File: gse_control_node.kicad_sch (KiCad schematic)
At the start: 5 parts

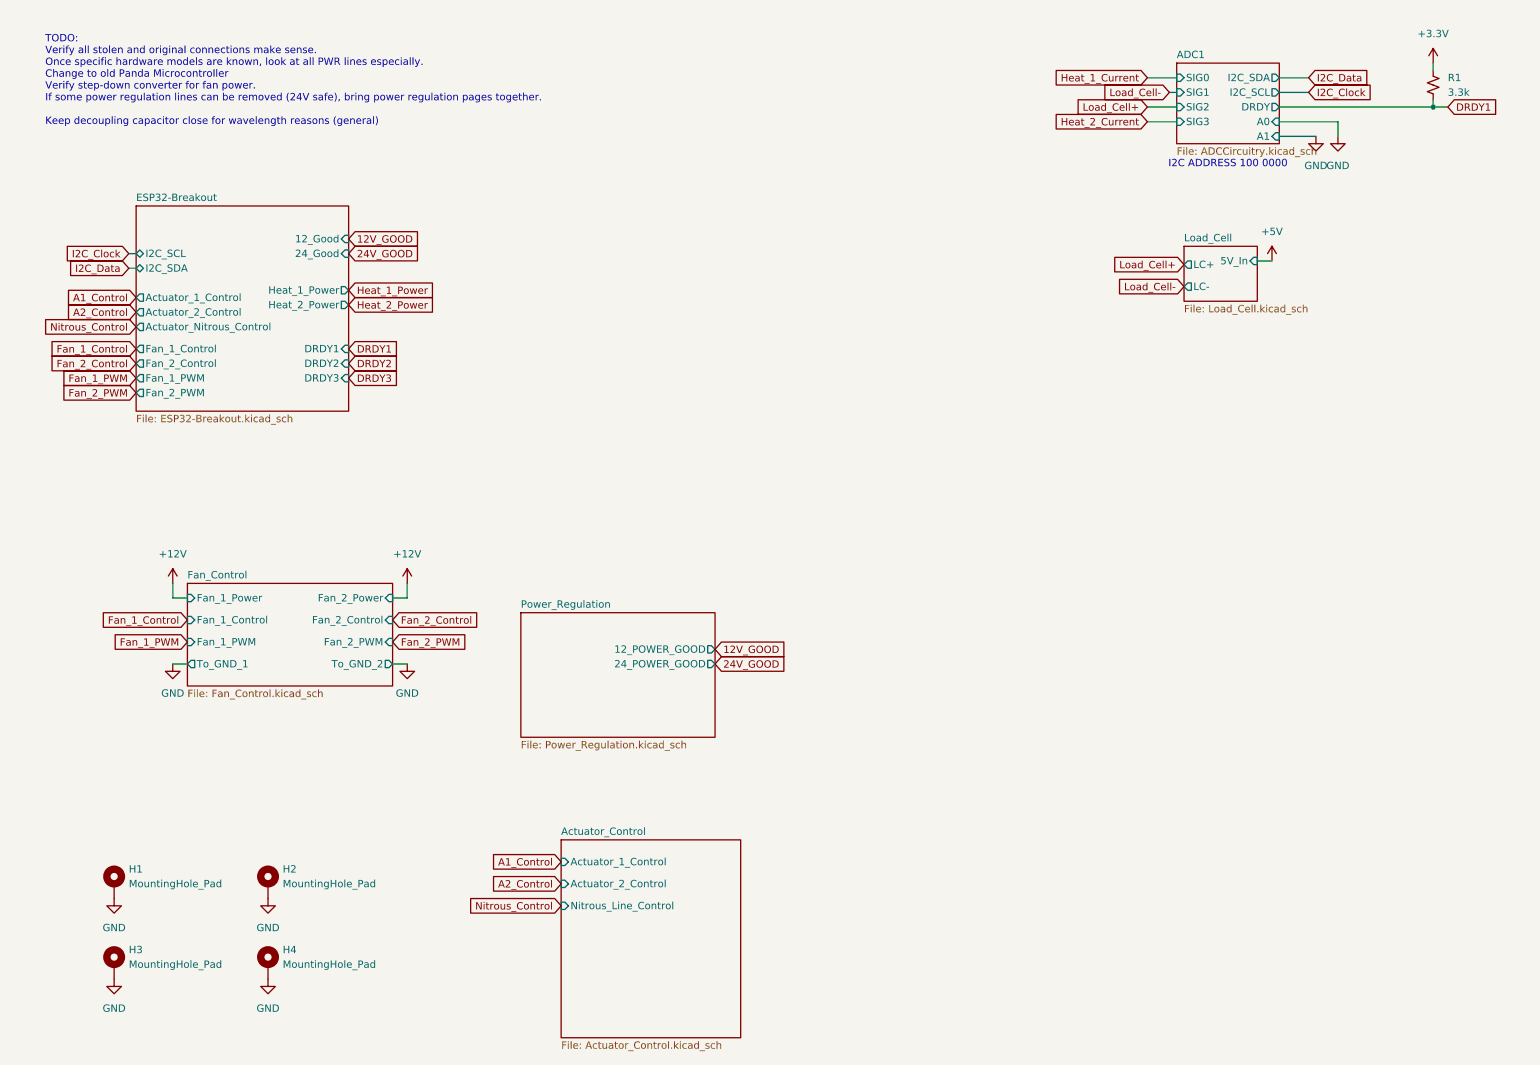
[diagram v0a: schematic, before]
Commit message: rename project to be more descriptive
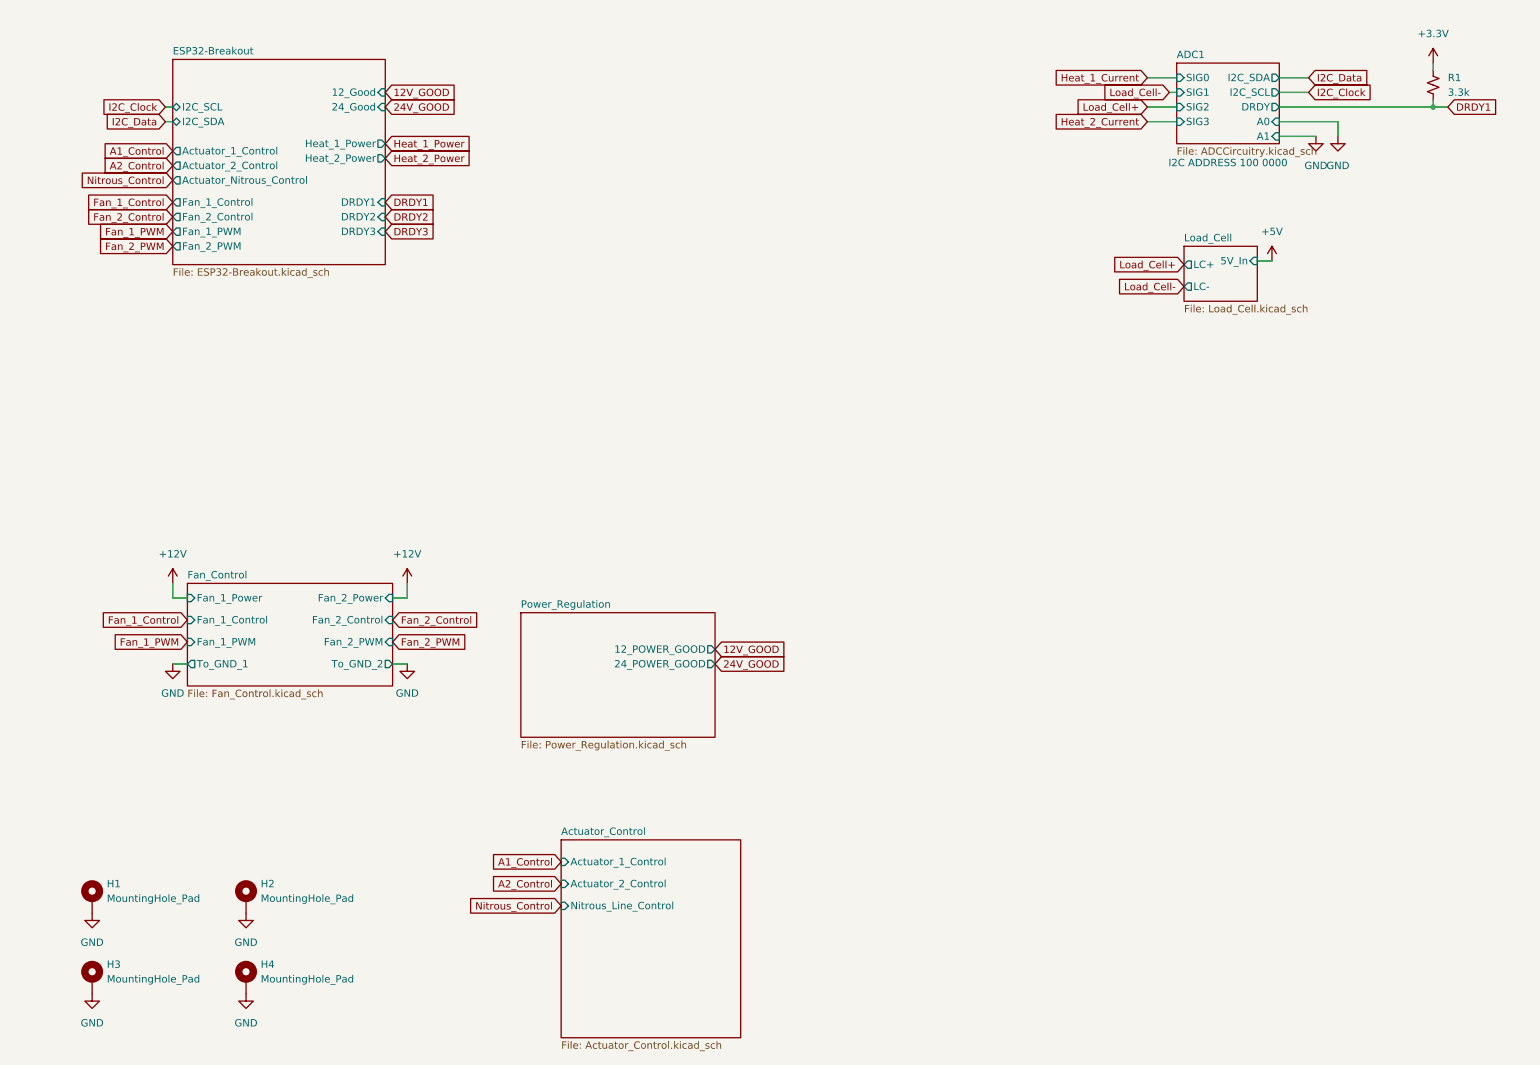
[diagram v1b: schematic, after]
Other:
- note removed: "TODO: Verify all stolen and original connections make sense. Once specific hardware models are known, look at all PWR lines especially. Change to old Panda Microcontroller Verify step-down converter for fan power. If some power regulation lines can be removed (24V safe), bring power regulation pages together. Keep decoupling capacitor close for wavelength reasons (general)"
- moved on the sheet: H1, H2, H3, H4

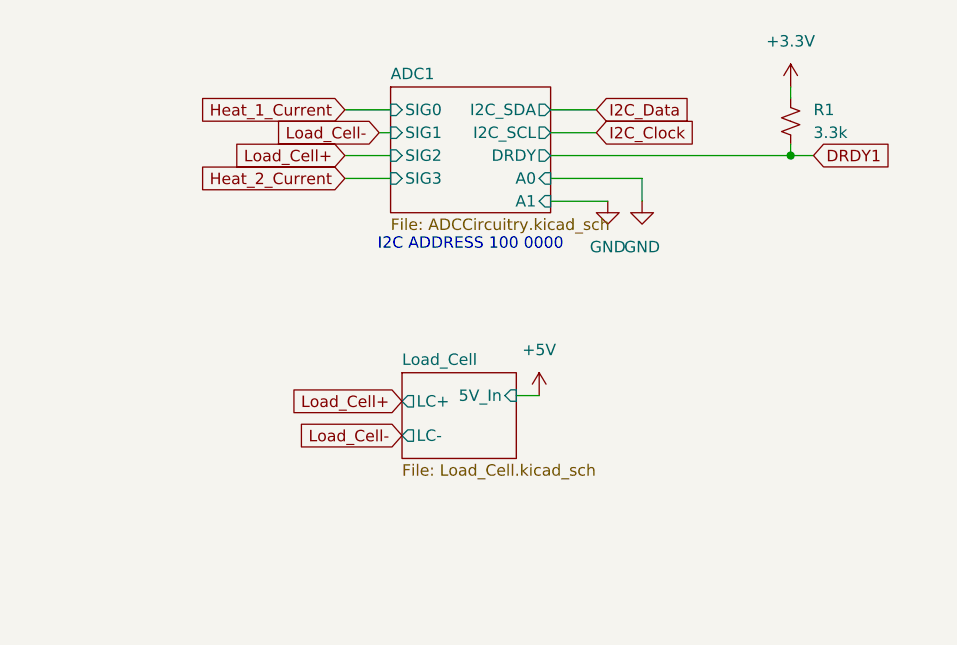
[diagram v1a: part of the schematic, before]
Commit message: fix load cell connector
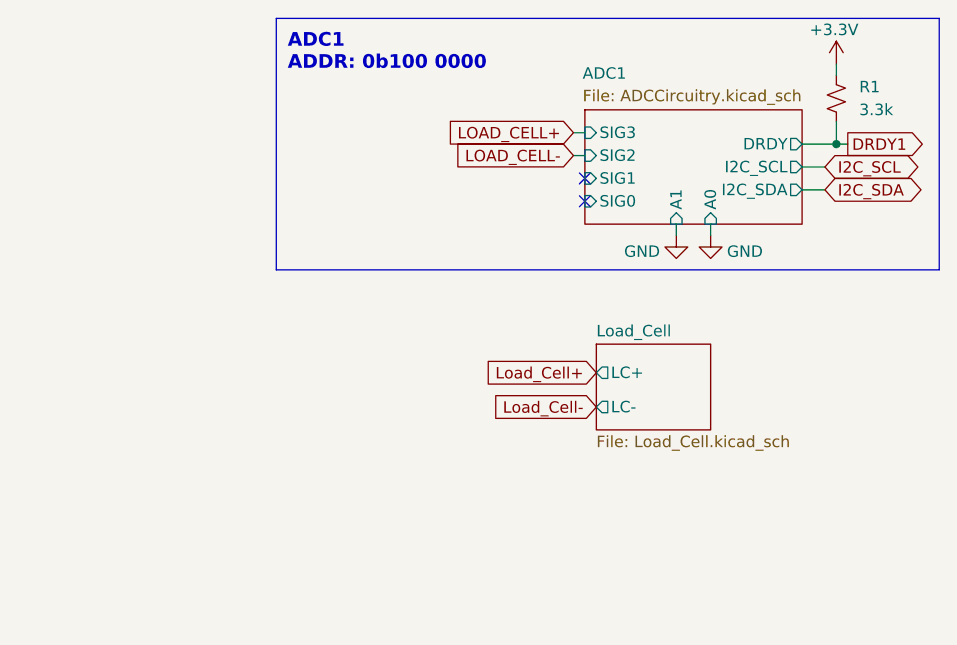
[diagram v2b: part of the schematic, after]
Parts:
- R1: LCSC (none) -> C25890; MPN (none) -> 0402WGF3301TCE
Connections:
- no-connect marks 0 -> 2
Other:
- sheet Load_Cell ports: added none; removed 5V_In
- note added: "ADC1 ADDR: 0b100 0000"
- note removed: "I2C ADDRESS 100 0000"

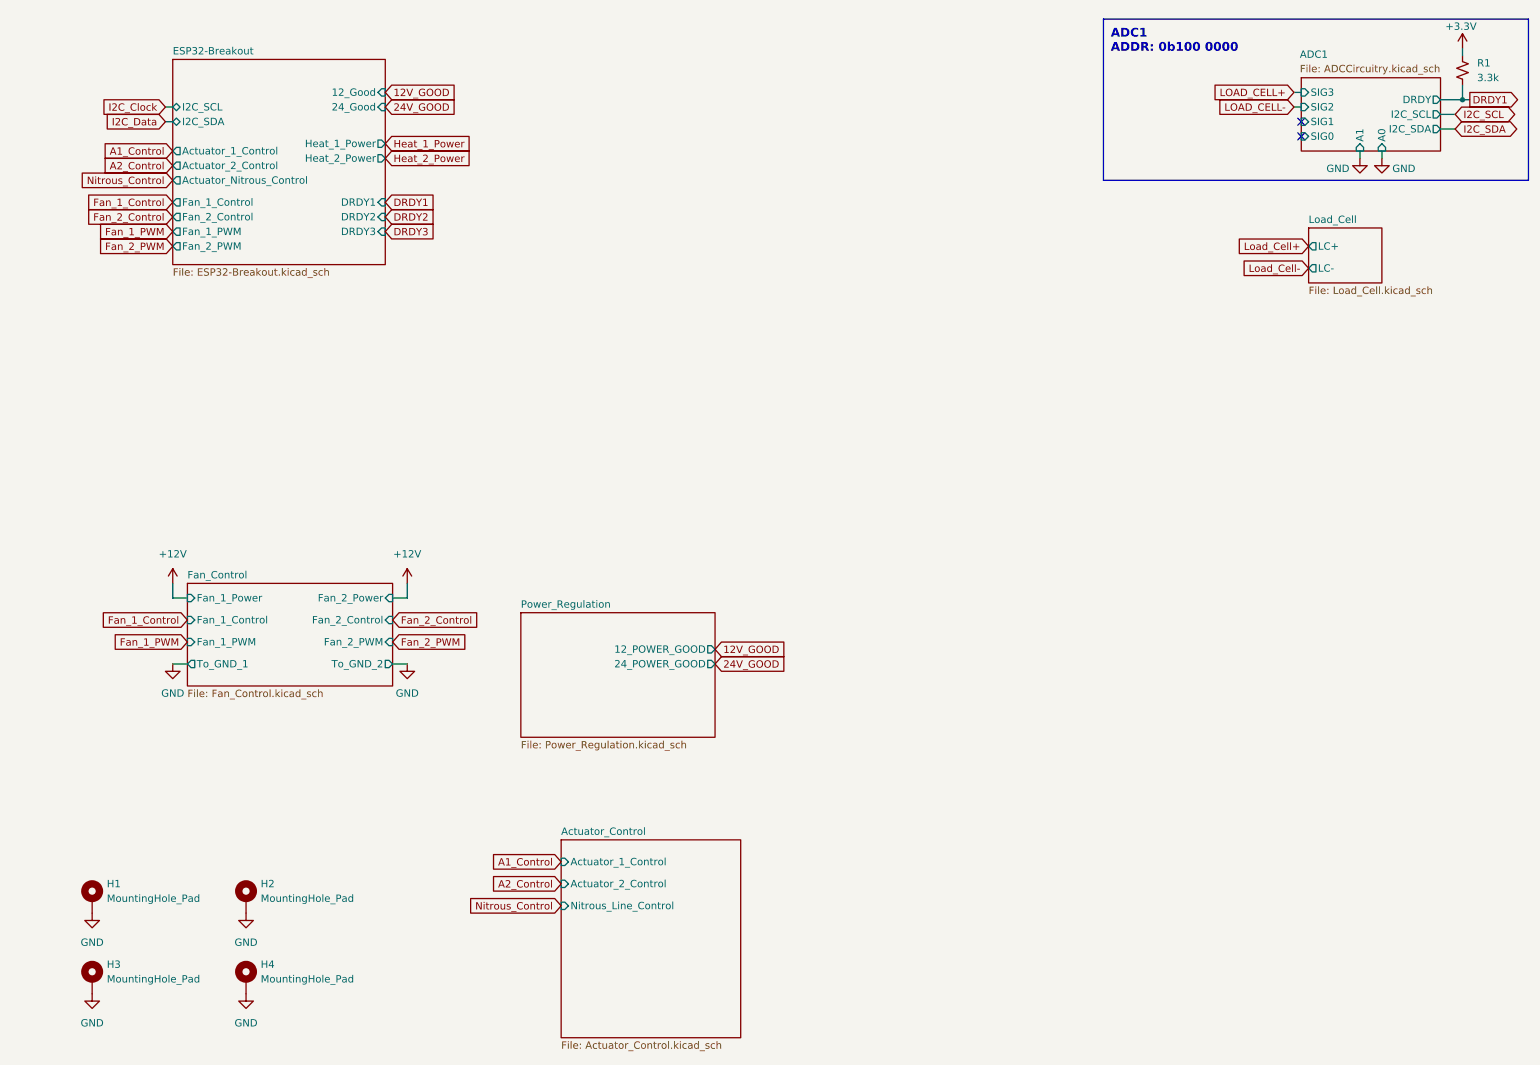
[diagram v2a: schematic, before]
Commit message: switch to on-board esp32s3
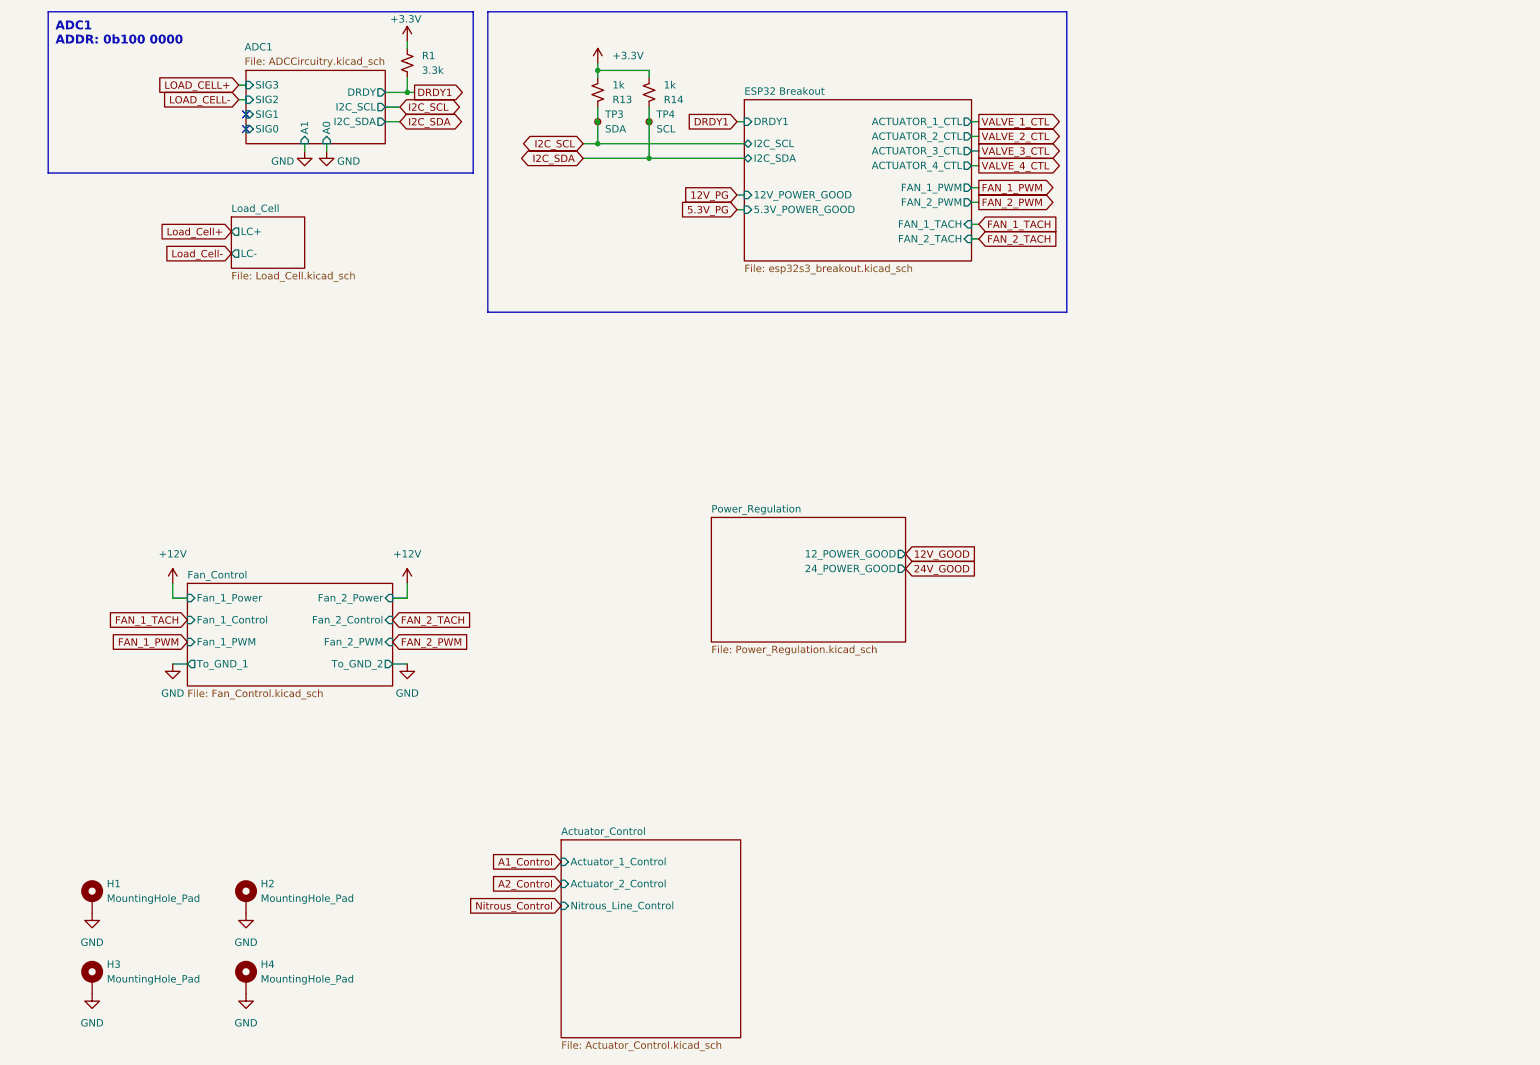
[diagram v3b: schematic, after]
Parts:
- added R13, R14: 1k, Resistor_SMD:R_0402_1005Metric, symbol Device:R_Small_US
- added TP3: SDA, TestPoint:TestPoint_Pad_D1.5mm, symbol Connector:TestPoint_Small
- added TP4: SCL, TestPoint:TestPoint_Pad_D1.5mm, symbol Connector:TestPoint_Small
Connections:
- net +3.3V: now also R13.2, R14.2
- net I2C_SCL: now also R13.1, TP3.1
- net I2C_SDA: now also R14.1, TP4.1
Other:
- removed sheet ESP32-Breakout
- added sheet ESP32 Breakout (esp32s3_breakout.kicad_sch)
- moved on the sheet: R1

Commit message: fix fan header footprint
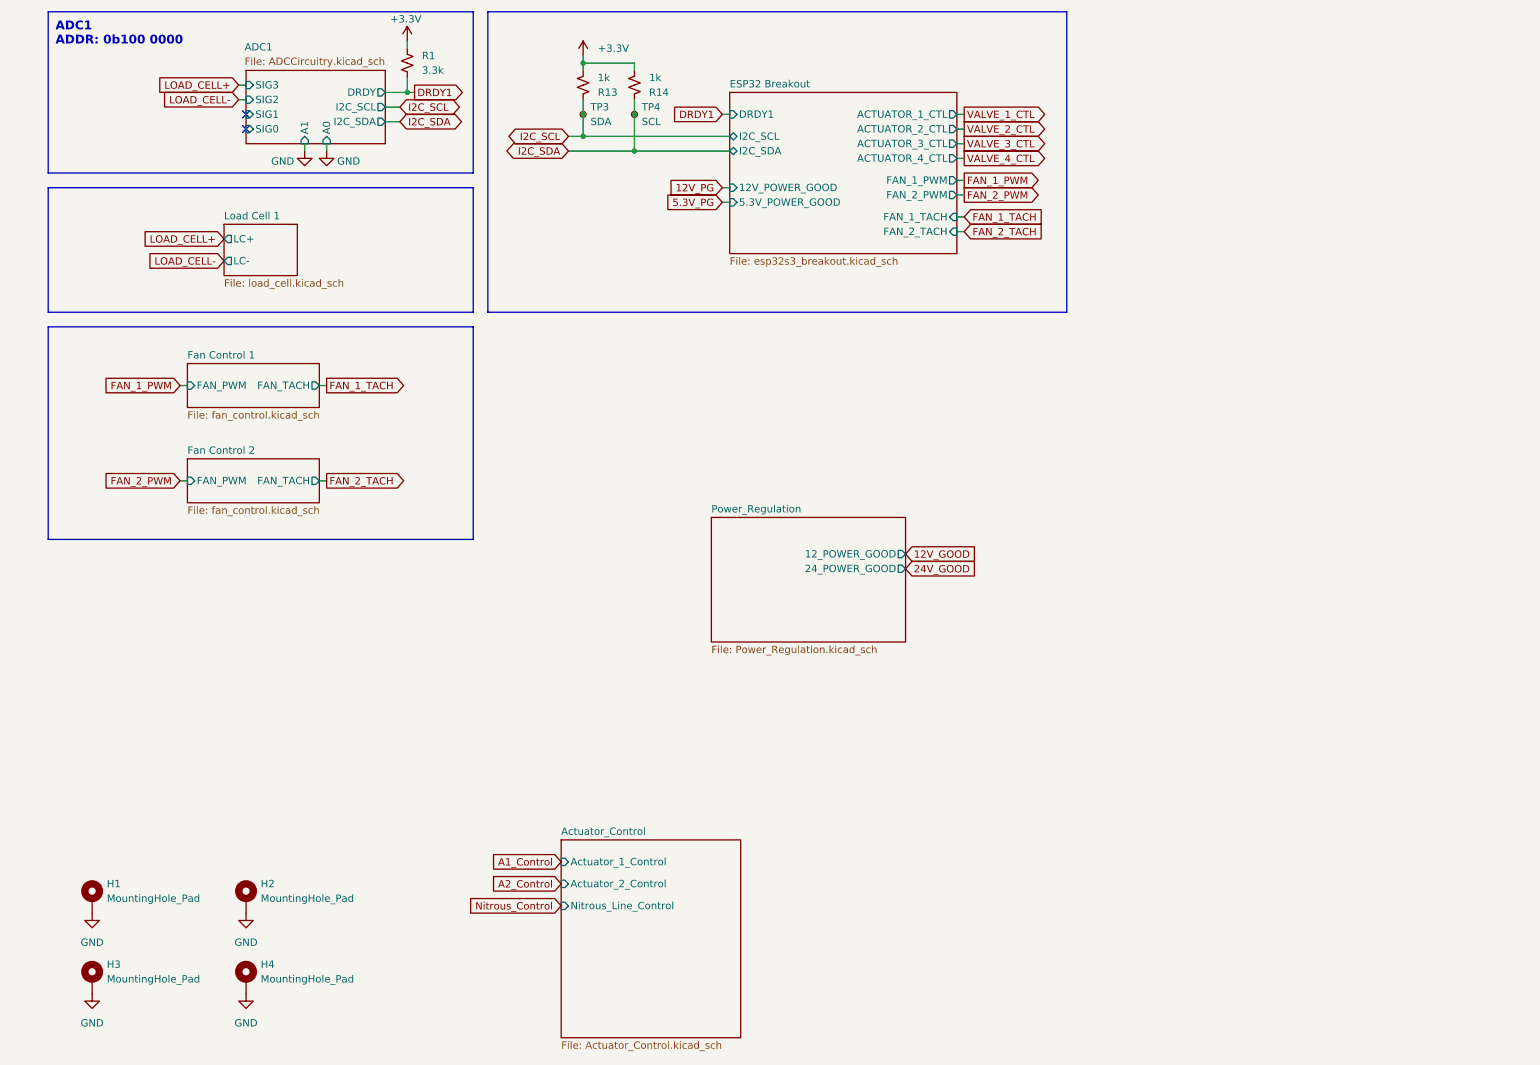
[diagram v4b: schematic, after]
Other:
- sheet Load_Cell renamed Load Cell 1
- removed sheet Fan_Control
- added sheet Fan Control 1 (fan_control.kicad_sch)
- added sheet Fan Control 2 (fan_control.kicad_sch)
- sheet Load Cell 1: file Load_Cell.kicad_sch -> load_cell.kicad_sch
- moved on the sheet: R13, R14, TP3, TP4
